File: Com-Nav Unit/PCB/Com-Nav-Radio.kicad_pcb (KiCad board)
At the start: 2 copper layers, 147 x 45 mm, 81 parts, among them J1 USB_C_Receptacle_USB2.0_14P, Q10 SS8550, Q11 SS8550, Q12 SS8550, Q13 SS8550, Q14 SS8550, Q15 SS8550, Q16 SS8550, Q2 SS8550, Q3 SS8550, Q4 SS8550, Q5 SS8550, Q6 SS8550, Q7 SS8550, Q8 SS8550, Q9 SS8550, SW1 EC12D1524403, SW2 EC12E1240301, SW3 EC12D1524403, SW4 EC12E1240301, U1 STM32F411CEUx, U2 74HC595, U3 74HC595, U4 XC6206P332MR, Y2 25 MHz

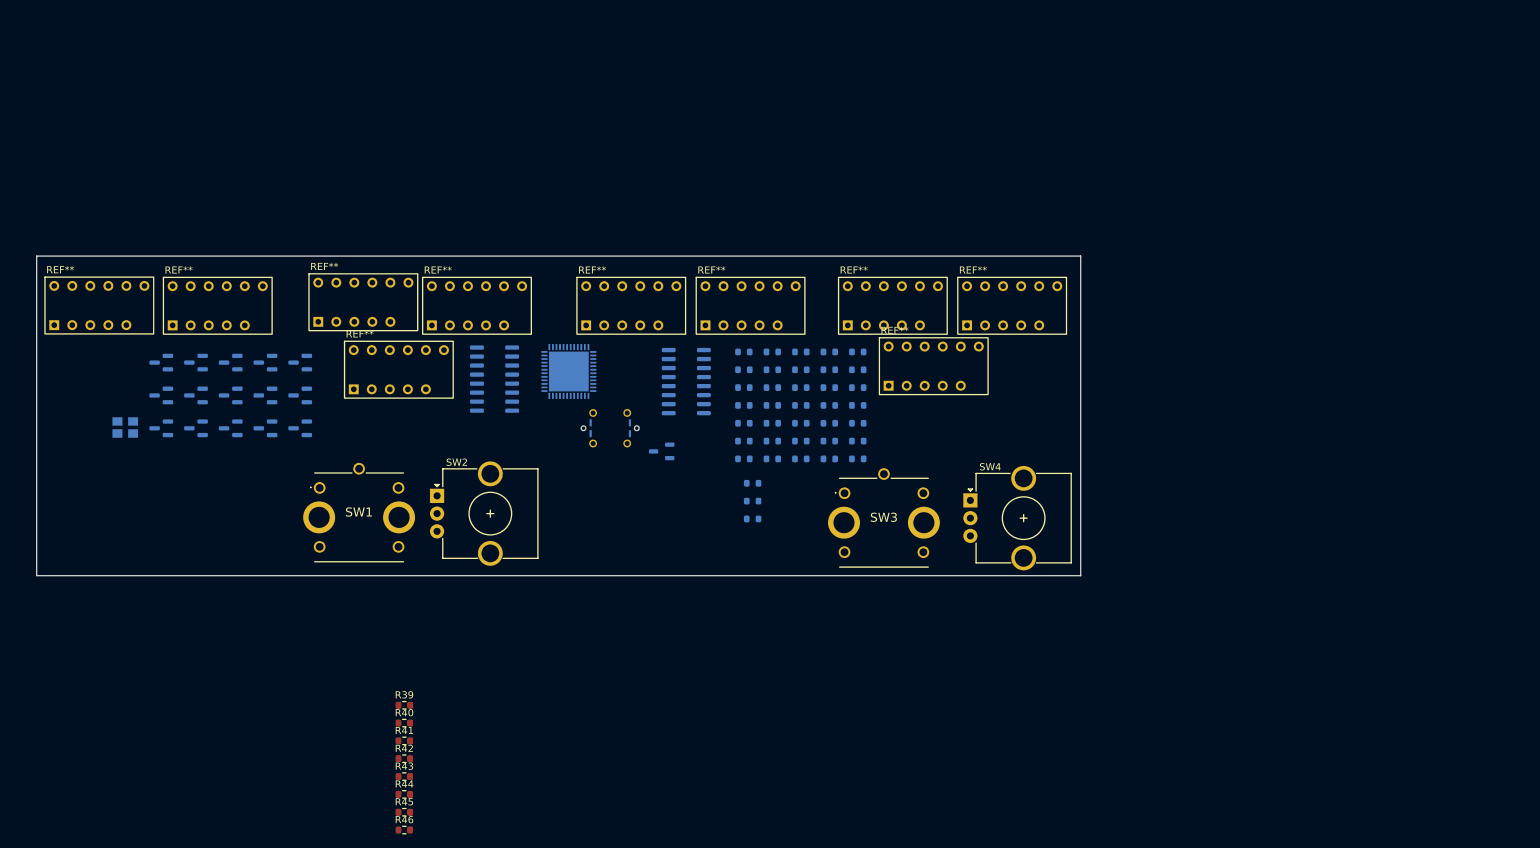
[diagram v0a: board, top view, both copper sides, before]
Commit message: PCB- Sch Connect 7 segments
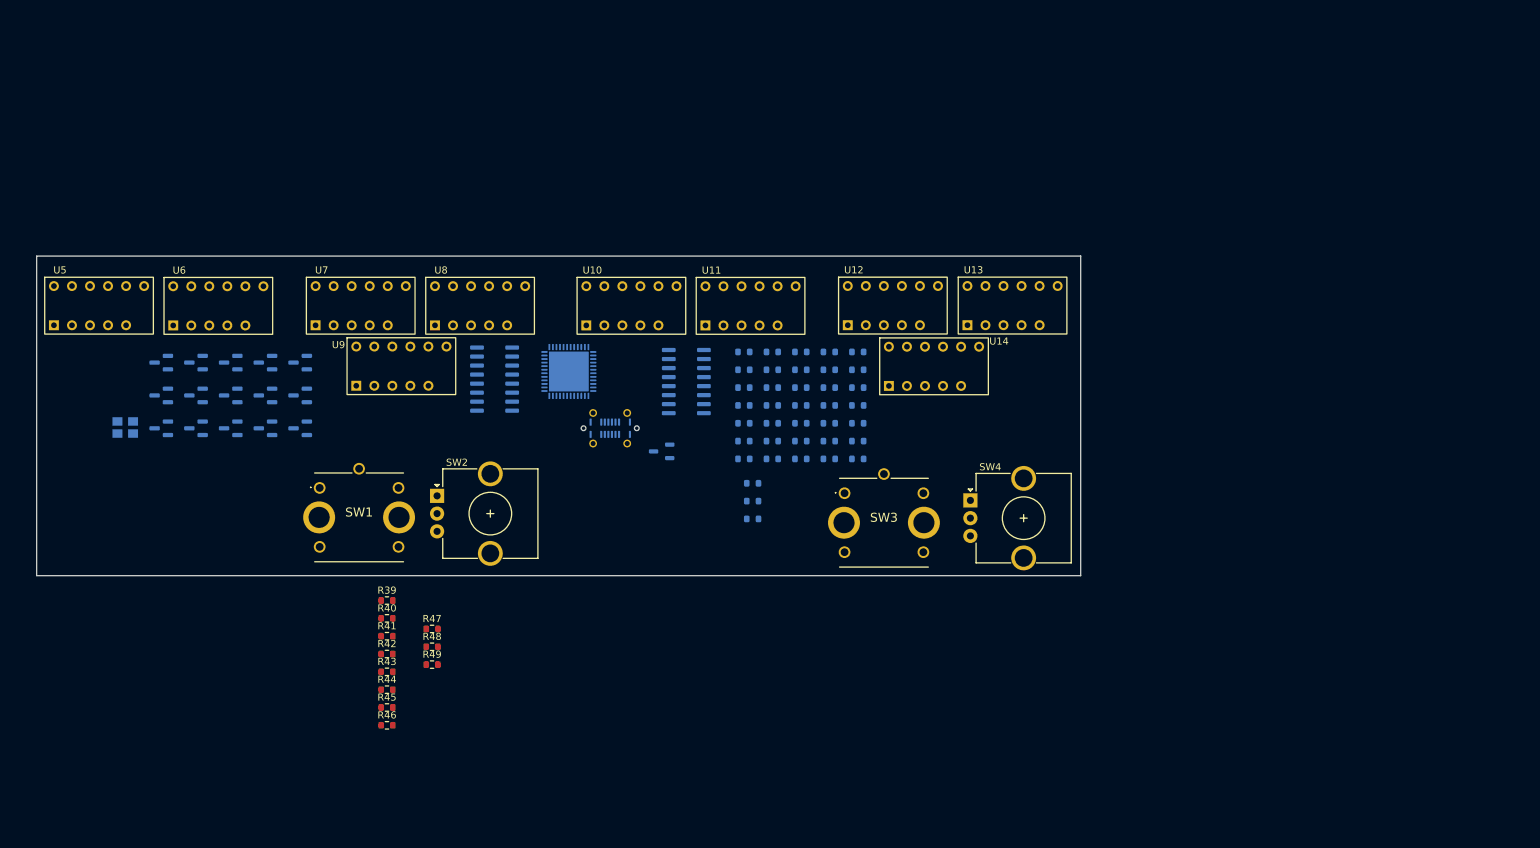
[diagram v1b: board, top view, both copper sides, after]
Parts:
- removed REF** (x10): FJ2352BH, Custom_7seg:FJ2352BH
- added R47: 5.1k, Resistor_SMD:R_0603_1608Metric, F.Cu at (134.2, 129.5)
- added R48: 5.1k, Resistor_SMD:R_0603_1608Metric, F.Cu at (134.2, 132.0)
- added R49: 0, Resistor_SMD:R_0603_1608Metric, F.Cu at (134.2, 134.5)
- added U10: FJ2352BH, Custom_7seg:FJ2352BH, F.Cu at (162.2, 84.0)
- added U11: FJ2352BH, Custom_7seg:FJ2352BH, F.Cu at (179.0, 84.0)
- added U12: FJ2352BH, Custom_7seg:FJ2352BH, F.Cu at (199.1, 84.0)
- added U13: FJ2352BH, Custom_7seg:FJ2352BH, F.Cu at (215.9, 84.0)
- added U14: FJ2352BH, Custom_7seg:FJ2352BH, F.Cu at (204.8, 92.5)
- added U5: FJ2352BH, Custom_7seg:FJ2352BH, F.Cu at (87.3, 84.0)
- added U6: FJ2352BH, Custom_7seg:FJ2352BH, F.Cu at (104.1, 84.0)
- added U7: FJ2352BH, Custom_7seg:FJ2352BH, F.Cu at (124.1, 84.0)
- added U8: FJ2352BH, Custom_7seg:FJ2352BH, F.Cu at (140.9, 84.0)
- added U9: FJ2352BH, Custom_7seg:FJ2352BH, F.Cu at (129.9, 92.5)
- J1: value USB_C_Receptacle_USB2.0_14P -> GT-USB-7055; footprint Connectors:USB_C_Receptacle_G-Switch_GT-USB-7051x -> Connectors:USB_C_Receptacle_G-Switch_GT-USB-7055x
- moved R39 14.9 mm to (127.8, 125.5)
- moved R40 14.9 mm to (127.8, 128.0)
- moved R42 14.9 mm to (127.8, 133.0)
- moved R43 14.9 mm to (127.8, 135.5)
- moved R45 14.9 mm to (127.8, 140.6)
- moved R46 14.9 mm to (127.8, 143.1)
- moved R41 14.9 mm to (127.8, 130.5)
- moved R44 14.9 mm to (127.8, 138.1)
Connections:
- J1 pad S1: unconnected-(J1-SHIELD-PadS1)_2 -> Net-(J1-SHIELD)
- Q10 pad 3: unconnected-(Q10-C-Pad3) -> /DIG9
- Q11 pad 3: unconnected-(Q11-C-Pad3) -> /DIG10
- Q12 pad 3: unconnected-(Q12-C-Pad3) -> /DIG11
- Q13 pad 3: unconnected-(Q13-C-Pad3) -> /DIG12
- Q14 pad 3: unconnected-(Q14-C-Pad3) -> /DIG13
- Q15 pad 3: unconnected-(Q15-C-Pad3) -> /DIG14
- Q16 pad 3: unconnected-(Q16-C-Pad3) -> /DIG15
- Q2 pad 3: unconnected-(Q2-C-Pad3) -> /DIG.1
- Q3 pad 3: unconnected-(Q3-C-Pad3) -> /DIG2
- Q4 pad 3: unconnected-(Q4-C-Pad3) -> /DIG3
- Q5 pad 3: unconnected-(Q5-C-Pad3) -> /DIG4
- Q6 pad 3: unconnected-(Q6-C-Pad3) -> /DIG5
- Q7 pad 3: unconnected-(Q7-C-Pad3) -> /DIG6
- Q8 pad 3: unconnected-(Q8-C-Pad3) -> /DIG7
- Q9 pad 3: unconnected-(Q9-C-Pad3) -> /DIG8
- U1 pad 32: unconnected-(U1-PA11-Pad32) -> /USB_D-
- U1 pad 33: unconnected-(U1-PA12-Pad33) -> /USB_D+

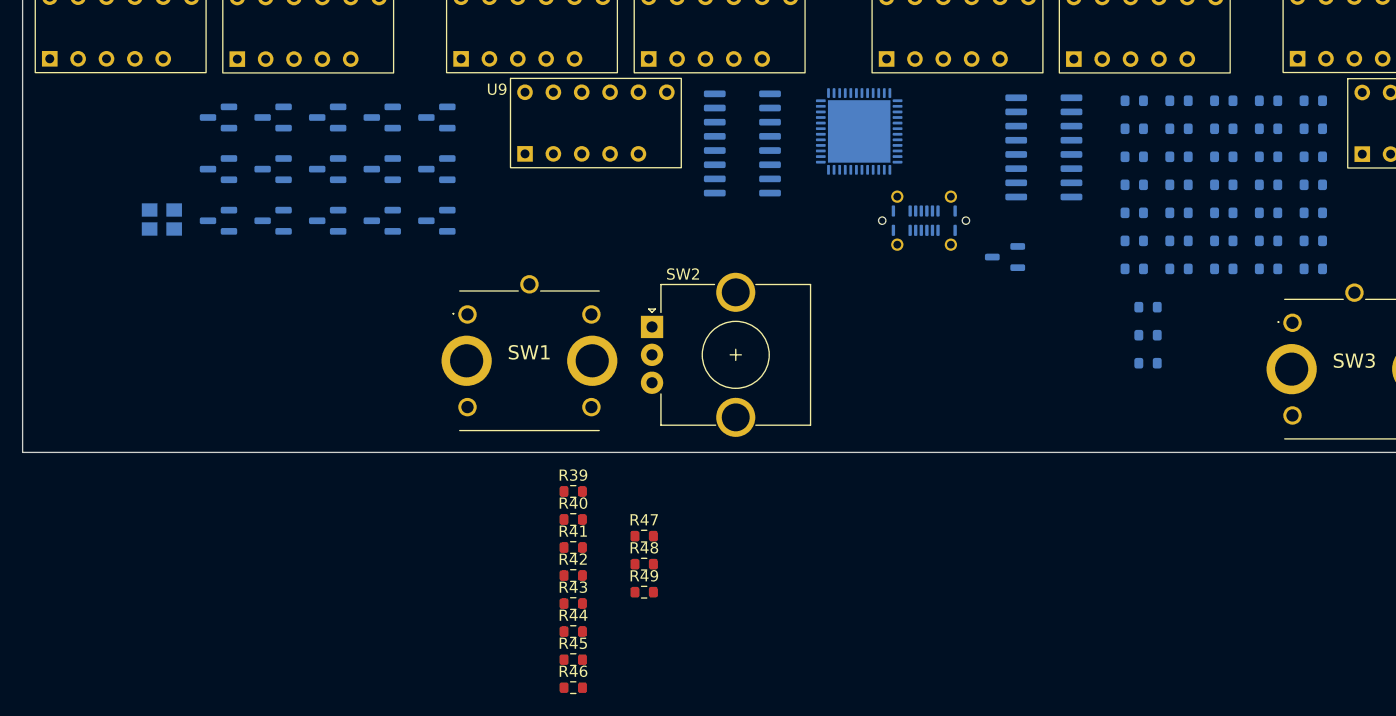
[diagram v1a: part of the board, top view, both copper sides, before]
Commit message: PCB - Add ferite bead, connect encoders
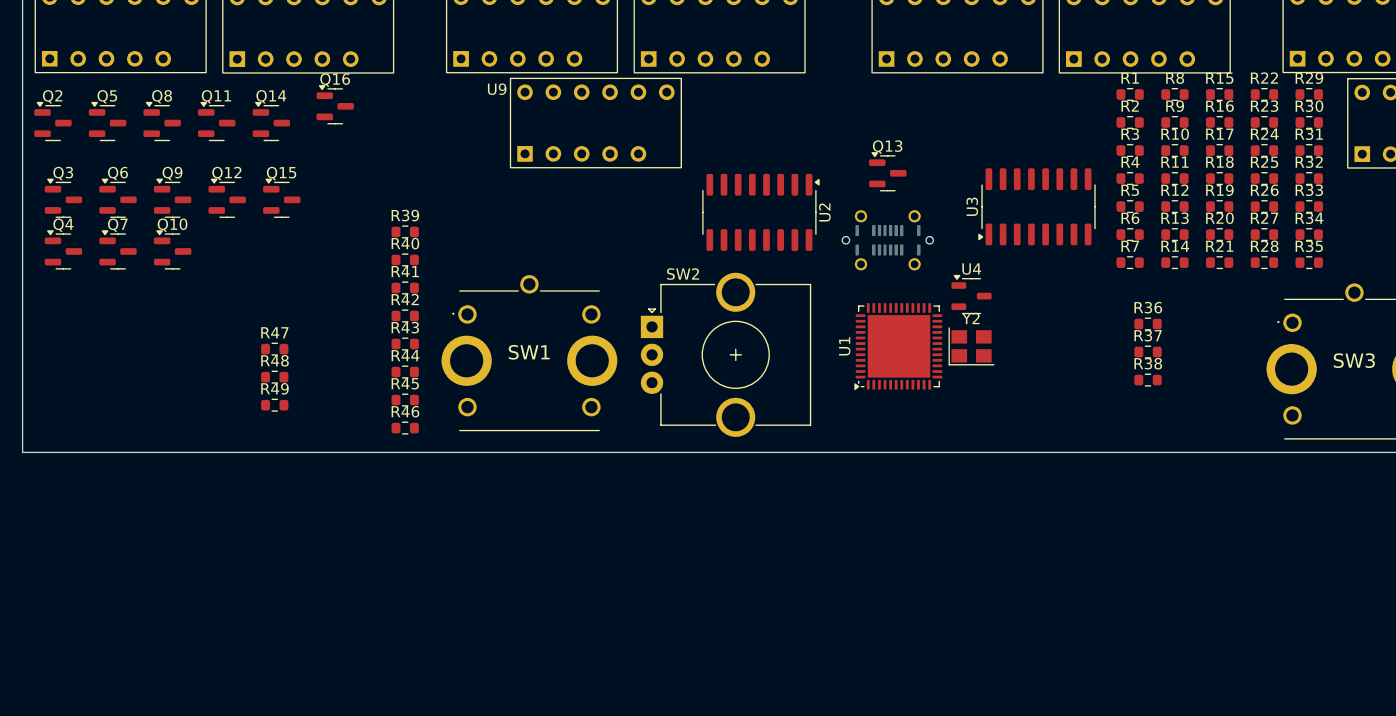
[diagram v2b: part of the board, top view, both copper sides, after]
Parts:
- Q10, Q11, Q12, Q13, Q14, Q15, Q16, Q2, Q3, Q4, Q5, Q6, Q7, Q8, Q9, R1, R10, R11, R12, R13, R14, R15, R16, R17, R18, R19, R2, R20, R21, R22, R23, R24, R25, R26, R27, R28, R29, R3, R30, R31, R32, R33, R34, R35, R36, R37, R38, R4, R5, R6, R7, R8, R9, U1, U2, U3, U4, Y2: moved to F.Cu
- moved Y2 73.4 mm to (163.5, 112.5), turned to 0 degrees
- moved Q13 55.2 mm to (156.0, 97.0), turned to 0 degrees
- moved R49 37.1 mm to (101.1, 117.8)
- moved R47 37.1 mm to (101.1, 112.8)
- moved R48 37.1 mm to (101.1, 115.3)
- moved Q2 34.4 mm to (81.2, 92.5), turned to 0 degrees
- moved Q3 33.6 mm to (82.2, 99.4), turned to 0 degrees
- moved Q4 33.6 mm to (82.2, 104.0), turned to 0 degrees
- moved R41 27.7 mm to (112.8, 107.3)
- moved R44 27.7 mm to (112.8, 114.8)
- moved R39 27.7 mm to (112.8, 102.2)
- moved R42 27.7 mm to (112.8, 109.8)
- moved R45 27.7 mm to (112.8, 117.3)
- moved R46 27.7 mm to (112.8, 119.8)
- moved R40 27.7 mm to (112.8, 104.8)
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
